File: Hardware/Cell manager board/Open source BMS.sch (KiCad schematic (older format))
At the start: 53 parts, among them P1 CONN_01X07, P2 EXT-TMP, P3 CONN_01X09, P4 CONN_01X09, Q1 BSS138, Q2 BSS138, Q3 BSS138, Q4 BSS138, Q5 BSS138, Q6 BSS138, U1 ATA6870N_BMS

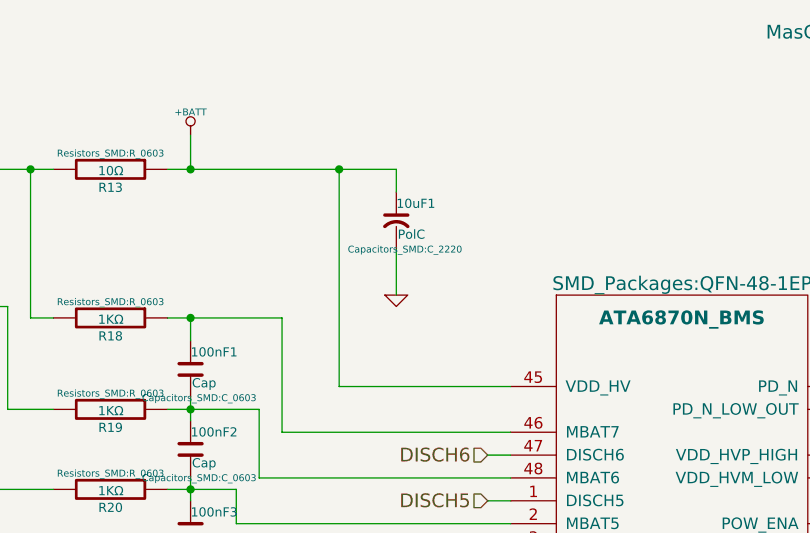
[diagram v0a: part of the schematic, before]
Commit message: Changed 10uf cap and added slave BOM
Changed the 10uf cap to one that is slightly smaller and 1/5th the
price. (at the expense of voltage, 100v>35v) Also added a BOM for the
Cell manager slave board with all parts but the thermistor and
assosiated resistors
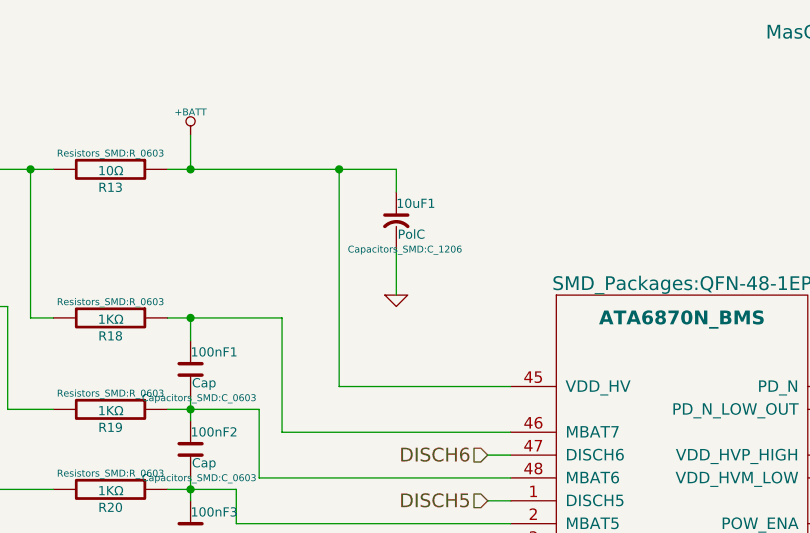
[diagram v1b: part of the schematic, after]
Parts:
- 10uF1: footprint Capacitors_SMD:C_2220 -> Capacitors_SMD:C_1206
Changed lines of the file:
@@
 F 0 "10uF1" H 6300 1600 40  0000 L CNN
 F 1 "PolC" H 6306 1465 40  0000 L CNN
-F 2 "Capacitors_SMD:C_2220" H 6338 1400 30  0000 C CNN
+F 2 "Capacitors_SMD:C_1206" H 6338 1400 30  0000 C CNN
 F 3 "" H 6150 1500 60  0000 C CNN
 	1    6300 1500

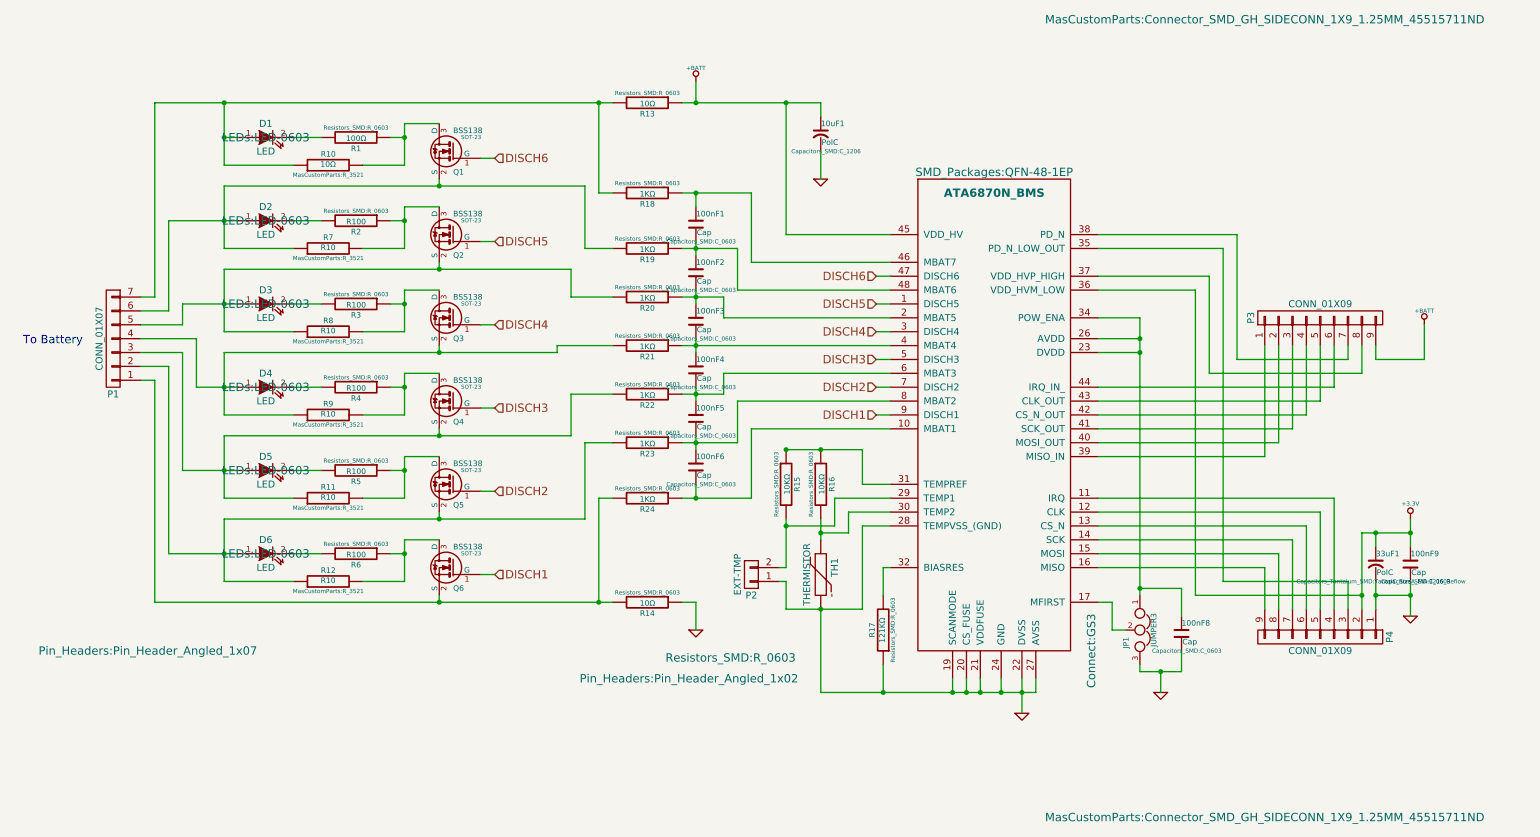
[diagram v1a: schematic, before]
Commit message: added schematic pictures and brushed up labels
ditto
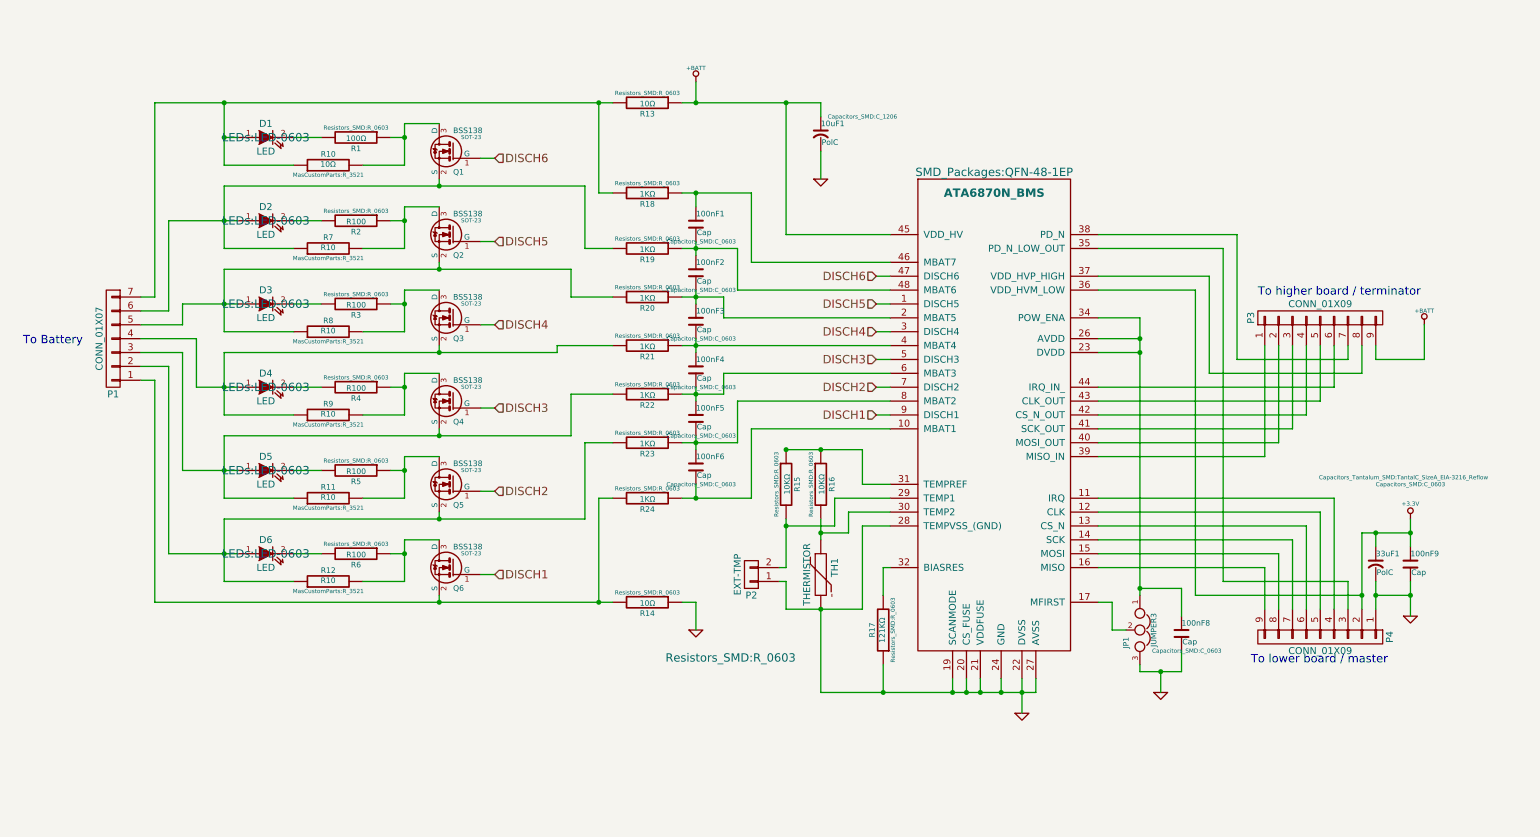
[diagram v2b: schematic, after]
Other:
- note added: "To higher board / terminator"
- note added: "To lower board / master"
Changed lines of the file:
@@
 F 0 "P1" H 1200 3350 50  0000 C CNN
 F 1 "CONN_01X07" V 1300 2950 50  0000 C CNN
-F 2 "Pin_Headers:Pin_Header_Angled_1x07" H 950 5200 60  0000 C CNN
+F 2 "Pin_Headers:Pin_Header_Angled_1x07" H 950 5200 60  0001 C CNN
 F 3 "" H 1200 2950 60  0000 C CNN
 	1    1200 2950
@@
 F 0 "P2" H 5800 4800 50  0000 C CNN
 F 1 "EXT-TMP" V 5900 4650 50  0000 C CNN
-F 2 "Pin_Headers:Pin_Header_Angled_1x02" H 6250 5400 60  0000 C CNN
+F 2 "Pin_Headers:Pin_Header_Angled_1x02" H 6250 5400 60  0001 C CNN
 F 3 "" H 5800 4650 60  0000 C CNN
 	1    5800 4650
@@
 F 0 "33uF1" H 10300 4700 40  0000 L CNN
 F 1 "PolC" H 10306 4565 40  0000 L CNN
-F 2 "Capacitors_Tantalum_SMD:TantalC_SizeA_EIA-3216_Reflow" H 10338 4500 30  0000 C CNN
+F 2 "Capacitors_Tantalum_SMD:TantalC_SizeA_EIA-3216_Reflow" H 10500 5250 30  0000 C CNN
 F 3 "" H 10150 4600 60  0000 C CNN
 	1    10300 4600
@@
 F 0 "P3" H 9900 3300 50  0000 C CNN
 F 1 "CONN_01X09" V 10000 2800 50  0000 C CNN
-F 2 "MasCustomParts:Connector_SMD_GH_SIDECONN_1X9_1.25MM_45515711ND" V 12050 3200 60  0000 C CNN
+F 2 "MasCustomParts:Connector_SMD_GH_SIDECONN_1X9_1.25MM_45515711ND" V 12050 3200 60  0001 C CNN
 F 3 "" H 9900 2800 60  0000 C CNN
 	1    9900 2800
@@
 F 0 "100nF9" H 10550 4700 40  0000 L CNN
 F 1 "Cap" H 10556 4565 40  0000 L CNN
-F 2 "Capacitors_SMD:C_0603" H 10588 4500 30  0000 C CNN
+F 2 "Capacitors_SMD:C_0603" H 10550 5200 30  0000 C CNN
 F 3 "" H 10400 4600 60  0000 C CNN
 	1    10550 4600
@@
 F 0 "10uF1" H 6300 1600 40  0000 L CNN
 F 1 "PolC" H 6306 1465 40  0000 L CNN
-F 2 "Capacitors_SMD:C_1206" H 6338 1400 30  0000 C CNN
+F 2 "Capacitors_SMD:C_1206" H 6600 1650 30  0000 C CNN
 F 3 "" H 6150 1500 60  0000 C CNN
 	1    6300 1500
@@
 F 0 "JP1" H 8650 4950 40  0000 L CNN
 F 1 "JUMPER3" H 8600 5150 40  0000 C CNN
-F 2 "Connect:GS3" H 8750 4700 60  0000 C CNN
+F 2 "Connect:GS3" H 8750 4700 60  0001 C CNN
 F 3 "" H 8600 5050 60  0000 C CNN
 	1    8600 5050
@@
 F 0 "P4" H 9900 5600 50  0000 C CNN
 F 1 "CONN_01X09" V 10000 5100 50  0000 C CNN
-F 2 "MasCustomParts:Connector_SMD_GH_SIDECONN_1X9_1.25MM_45515711ND" V 11200 4700 60  0000 C CNN
+F 2 "MasCustomParts:Connector_SMD_GH_SIDECONN_1X9_1.25MM_45515711ND" V 11200 4700 60  0001 C CNN
 F 3 "" H 9900 5100 60  0000 C CNN
 	1    9900 5100
 	0    1    1    0
 $EndComp
+Text Notes 9400 5300 0    60   ~ 0
+To lower board / master
+Text Notes 9450 2650 0    60   ~ 0
+To higher board / terminator
 $EndSCHEMATC
